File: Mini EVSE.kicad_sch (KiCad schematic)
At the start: 33 parts, among them IC1 G3MC-201PL DC5, IC2 IRM-03-5, IC3 ATtiny84-20P, IC4 TMR1-0522, IC5 SI8261BAC-C-IP, J1 RE OUT, J10 M, J2 AC IN, J4 ICP, J5 SWITCH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

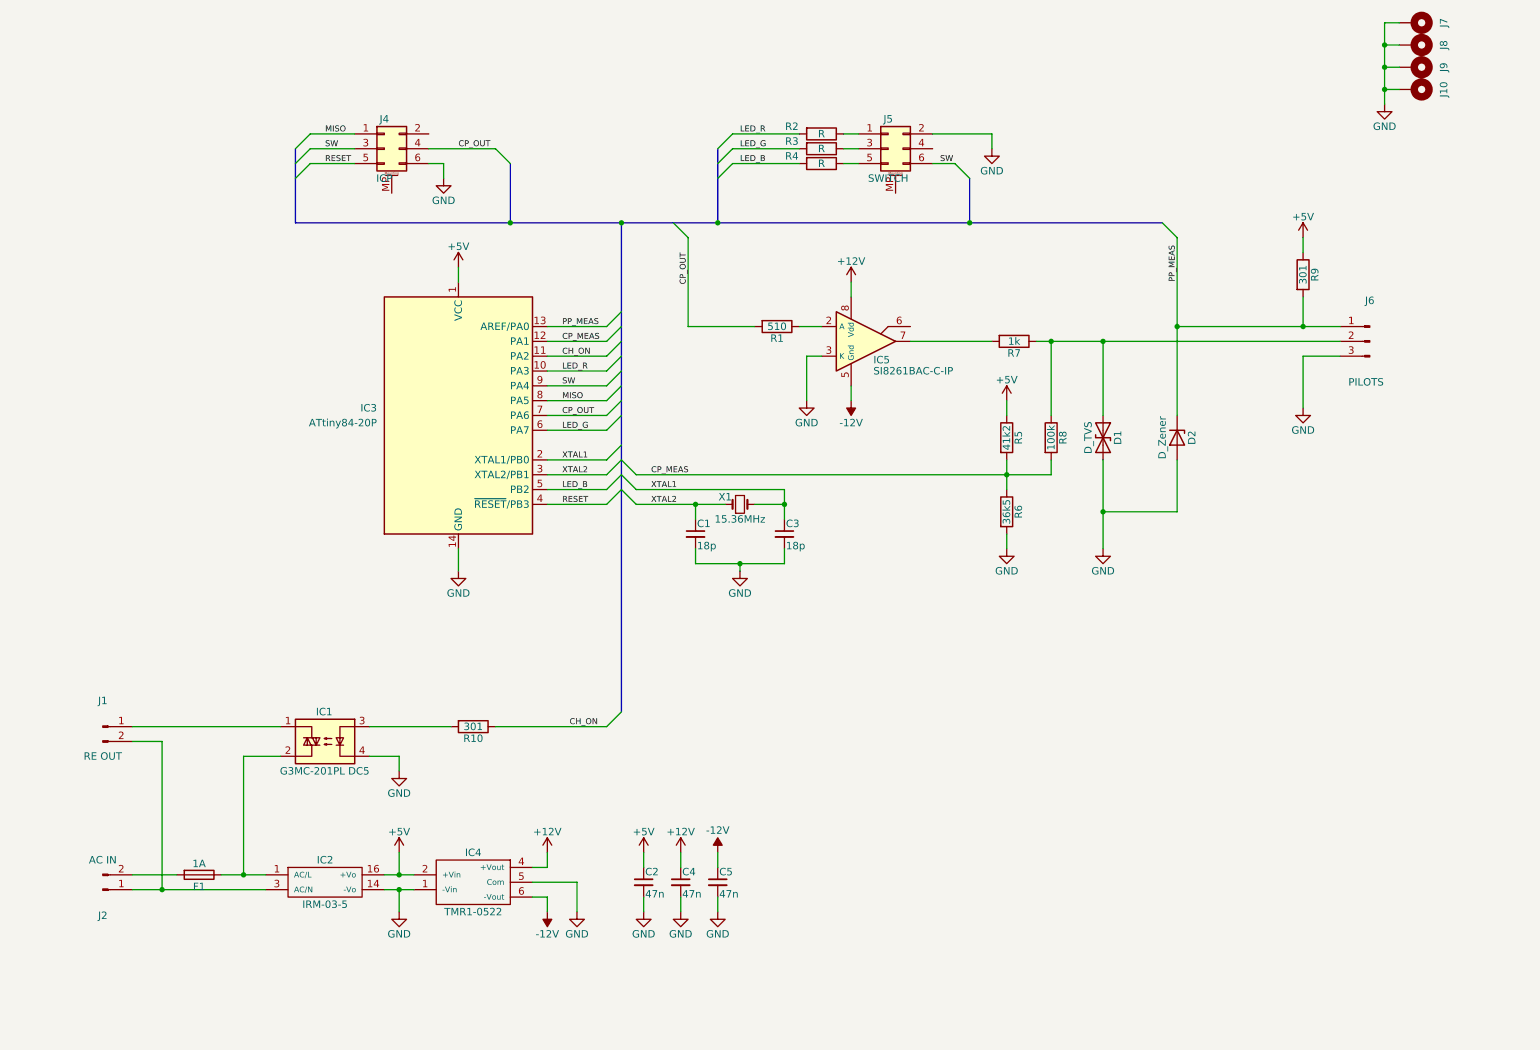
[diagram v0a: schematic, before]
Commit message: Changed supply to 24VDC with isolation
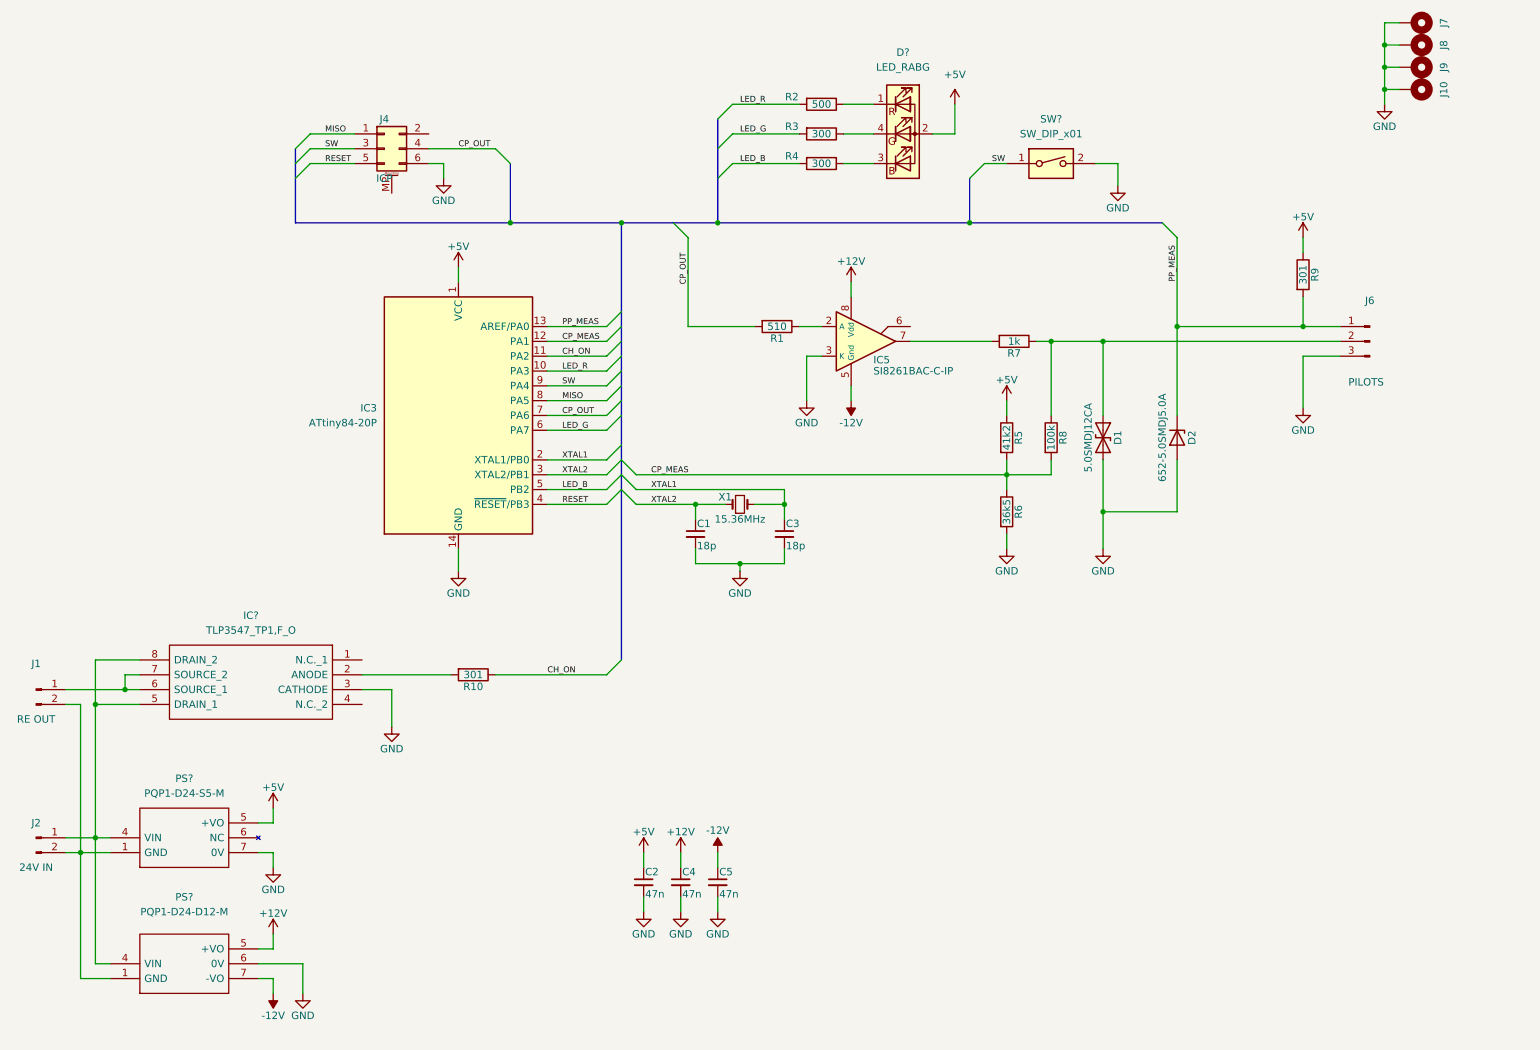
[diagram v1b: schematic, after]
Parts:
- removed F1: 1A, Fuse_Holders_and_Fuses:Fuseholder_Fuse_TR5_Littlefuse-No560_No460, symbol Device:Fuse
- removed IC1: G3MC-201PL DC5, Package_SIP:SIP4_Sharp-SSR_P7.62mm_Straight, symbol Relay_SolidState:S102S01
- removed IC2: IRM-03-5, Miscellaneous:MeanWell_IRM, symbol miscellaneous:IRM-03-5
- removed IC4: TMR1-0522, symbol miscellaneous:TMR1-0522
- removed J5: SWITCH, Pin_Headers:Pin_Header_Straight_2x03_Pitch2.54mm, symbol Connector_Generic_MountingPin:Conn_02x03_Odd_Even_MountingPin
- added D?: LED_RABG, symbol Device:LED_RABG
- added IC?: TLP3547_TP1,F_O, SOP254P1000X425-8N, symbol SamacSys_Parts:TLP3547_TP1,F_O
- added PS?: PQP1-D24-S5-M, PQP1D24S5M, symbol SamacSys_Parts:PQP1-D24-S5-M
- added PS?: PQP1-D24-D12-M, PQP1D24S5M, symbol SamacSys_Parts:PQP1-D24-S5-M
- added SW?: SW_DIP_x01, symbol Switch:SW_DIP_x01
- D1: value D_TVS -> 5.0SMDJ12CA
- D2: value D_Zener -> 652-5.0SMDJ5.0A
- J2: value AC IN -> 24V IN
- R2: value R -> 500
- R3, R4: value R -> 300
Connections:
- net +12V: now also PS?.5 (+VO)
- net +5V: now also D?.2 (A), PS?.5 (+VO)
- net -12V: now also PS?.7 (-VO)
- net GND: now also IC?.3 (CATHODE), PS?.6 (0V), PS?.7 (0V), SW?.2
- net SW: now also SW?.1
- net at J2.1 (Pin_1): now also IC?.5 (DRAIN_1), IC?.8 (DRAIN_2), PS?.4 (VIN), PS?.4 (VIN); no longer J1.2 (Pin_2)
- net at J2.2 (Pin_2): now also J1.2 (Pin_2), PS?.1 (GND), PS?.1 (GND)
- net at R2.1: now also D?.1 (RK)
- net at R3.1: now also D?.4 (GK)
- net at R4.1: now also D?.3 (BK)
- net at J1.1 (Pin_1): now also IC?.6 (SOURCE_1), IC?.7 (SOURCE_2)
- net at R10.2: now also IC?.2 (ANODE)
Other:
- moved on the sheet: J1, J2, R10, R2, R3

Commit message: Added PCB layout for DIN rail version
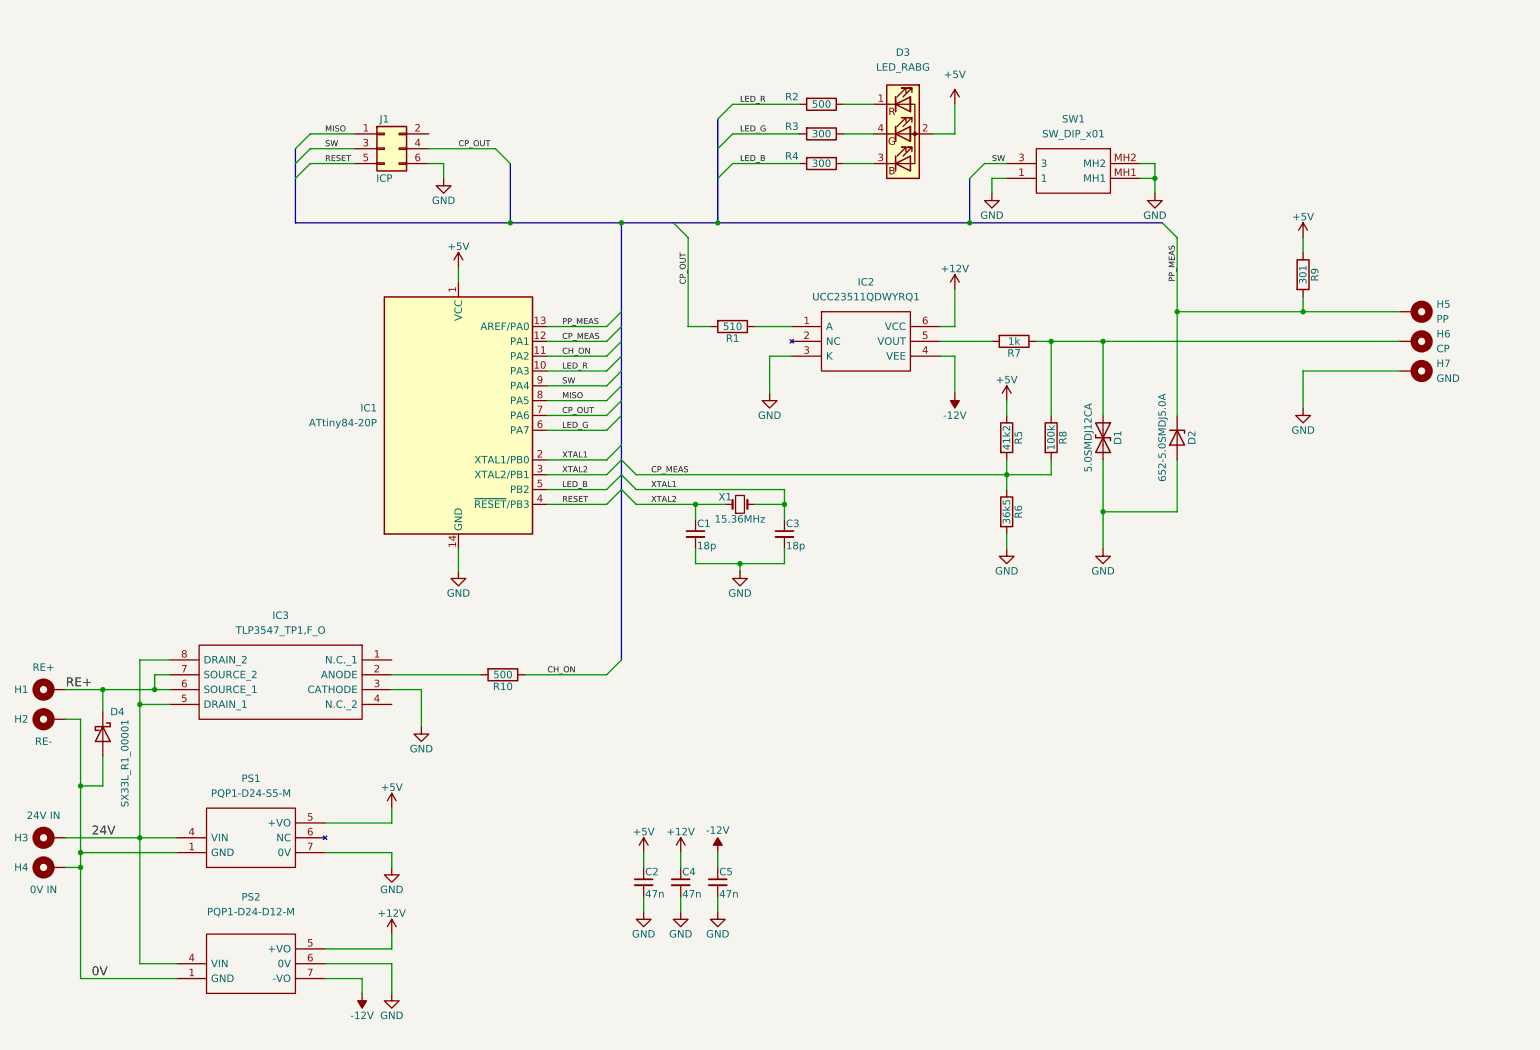
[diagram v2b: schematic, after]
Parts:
- removed IC5: SI8261BAC-C-IP, Housings_DIP:DIP-8_W7.62mm_LongPads, symbol miscellaneous:SI8261BAC-C-IP
- removed J1: RE OUT, Connectors_Terminal_Blocks:TerminalBlock_Pheonix_MKDS1.5-2pol, symbol Connector:Conn_01x02_Male
- removed J10, J7, J8, J9: M, Mounting_Holes:MountingHole_3.2mm_M3_ISO7380_Pad, symbol Mechanical:MountingHole_Pad
- removed J2: 24V IN, Connectors_Terminal_Blocks:TerminalBlock_Pheonix_MKDS1.5-2pol, symbol Connector:Conn_01x02_Male
- removed J6: PILOTS, Connectors_Terminal_Blocks:TerminalBlock_Pheonix_MKDS1.5-3pol, symbol Connector:Conn_01x03_Male
- added D4: SX33L_R1_00001, Diode_SMD:D_SMA_Handsoldering, symbol Device:D_Schottky
- added H1: RE+, TestPoint:TestPoint_Loop_D2.60mm_Drill1.4mm_Beaded, symbol Mechanical:MountingHole_Pad
- added H2: RE-, TestPoint:TestPoint_Loop_D2.60mm_Drill1.4mm_Beaded, symbol Mechanical:MountingHole_Pad
- added H3: 24V IN, TestPoint:TestPoint_Loop_D2.60mm_Drill1.4mm_Beaded, symbol Mechanical:MountingHole_Pad
- added H4: 0V IN, TestPoint:TestPoint_Loop_D2.60mm_Drill1.4mm_Beaded, symbol Mechanical:MountingHole_Pad
- added H5: PP, TestPoint:TestPoint_Loop_D2.60mm_Drill1.4mm_Beaded, symbol Mechanical:MountingHole_Pad
- added H6: CP, TestPoint:TestPoint_Loop_D2.60mm_Drill1.4mm_Beaded, symbol Mechanical:MountingHole_Pad
- added H7: GND, TestPoint:TestPoint_Loop_D2.60mm_Drill1.4mm_Beaded, symbol Mechanical:MountingHole_Pad
- added IC2: UCC23511QDWYRQ1, SamacSys_Parts:SOIC127P1150X355-6N, symbol SamacSys_Parts:UCC23511QDWYRQ1
- C1, C3: footprint Miscellaneous:C_Disc_D2.5mm_W3.2mm_P2.54mm -> Capacitor_SMD:C_1206_3216Metric_Pad1.33x1.80mm_HandSolder
- C2, C4, C5: footprint Miscellaneous:C_Disc_D5.1mm_W3.2mm_P5.08mm -> Capacitor_SMD:C_1206_3216Metric_Pad1.33x1.80mm_HandSolder
- D1, D2: footprint Diodes_THT:D_DO-201_P5.08mm_Vertical_KathodeUp -> Diode_SMD:D_SMC
- D3: renamed from D?; footprint (none) -> SamacSys_Parts:5504013F
- IC1: renamed from IC3; footprint Package_DIP:DIP-14_W7.62mm -> Package_SO:SOIC-14_3.9x8.7mm_P1.27mm
- IC3: renamed from IC?; footprint SOP254P1000X425-8N -> SamacSys_Parts:SOP254P1000X425-8N
- J1: renamed from J4; footprint Pin_Headers:Pin_Header_Straight_2x03_Pitch2.54mm -> Connector_PinHeader_2.54mm:PinHeader_2x03_P2.54mm_Vertical; symbol Connector_Generic_MountingPin:Conn_02x03_Odd_Even_MountingPin -> Connector_Generic:Conn_02x03_Odd_Even
- PS1, PS2: renamed from PS?; footprint PQP1D24S5M -> SamacSys_Parts:PQP1D24S5M
- R1, R2, R3, R4, R5, R6, R7, R8, R9: footprint Miscellaneous:R_Axial_DIN0207_L6.3mm_D2.5mm_P10.16mm_Horizontal -> Resistor_SMD:R_1210_3225Metric_Pad1.30x2.65mm_HandSolder
- R10: value 301 -> 500; footprint Miscellaneous:R_Axial_DIN0207_L6.3mm_D2.5mm_P10.16mm_Horizontal -> Resistor_SMD:R_1210_3225Metric_Pad1.30x2.65mm_HandSolder
- SW1: renamed from SW?; footprint (none) -> SamacSys_Parts:TPA11CGRA004; symbol Switch:SW_DIP_x01 -> SamacSys_Parts:TPA11CGRA004; Height (none) -> 5.994; Manufacturer_Name (none) -> TE Connectivity; Manufacturer_Part_Number (none) -> TPA11CGRA004; Mouser Part Number (none) -> 506-TPA11CGRA004; Mouser Price/Stock (none) -> https://www.mouser.co.uk/ProductDetail/TE-Connectivity-PB/T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
- X1: footprint Crystals:Crystal_HC49-U_Vertical -> Crystal:Crystal_HC49-U_Vertical
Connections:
- net +12V: now also IC2.6 (VCC)
- net -12V: now also IC2.4 (VEE)
- net GND: now also SW1.1, SW1.MH1, SW1.MH2, H7.1, IC2.3 (K); no longer SW1.2
- net PP_MEAS: now also H5.1
- net SW: now also SW1.3; no longer SW1.1
- net at R1.1: now also IC2.1 (A)
- net at R7.2: now also IC2.5 (VOUT)
- net at D1.1 (A1), R7.1, R8.1: now also H6.1
- net 24V: now reaches IC3.5 (DRAIN_1), IC3.8 (DRAIN_2), PS1.4 (VIN), PS2.4 (VIN)
- net 24V: now also H3.1
- net 0V: now reaches PS1.1 (GND), PS2.1 (GND)
- net 0V: now also D4.2 (A), H2.1, H4.1
- net RE+: now reaches IC3.6 (SOURCE_1), IC3.7 (SOURCE_2)
- net RE+: now also D4.1 (K), H1.1
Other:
- moved on the sheet: IC3, PS1, PS2, R1, R10

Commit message: Fixes to PCB layout - first prototype
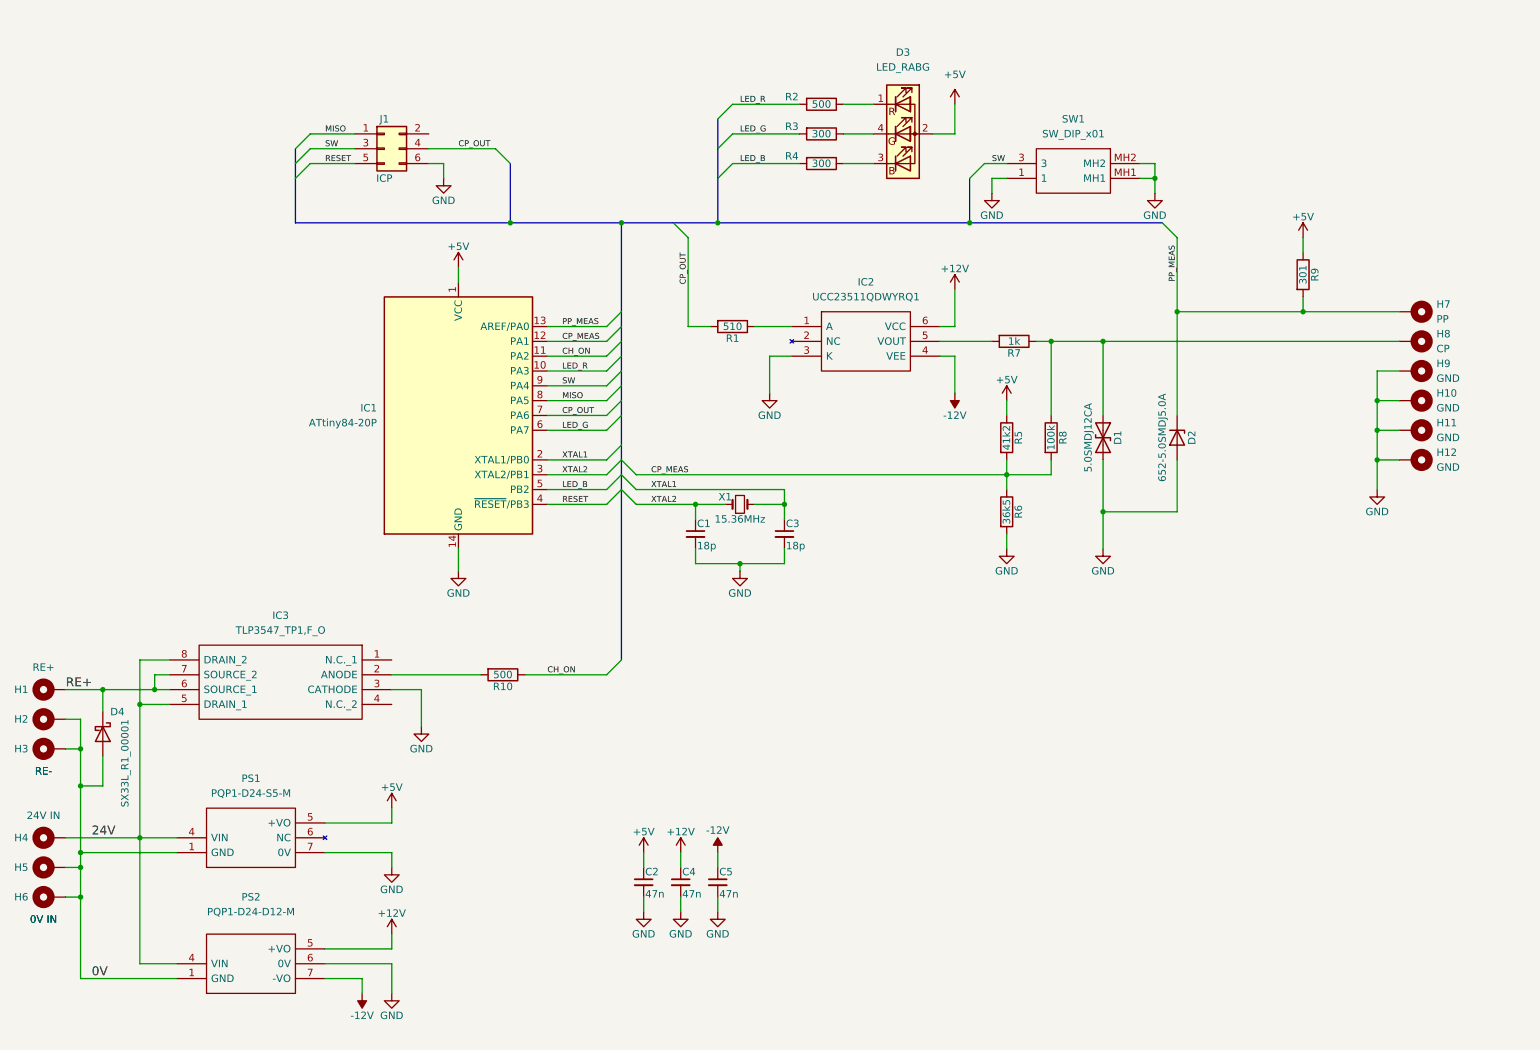
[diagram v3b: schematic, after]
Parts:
- added H10, H11, H12: GND, TestPoint:TestPoint_Loop_D2.60mm_Drill1.4mm_Beaded, symbol Mechanical:MountingHole_Pad
- added H3: RE-, TestPoint:TestPoint_Loop_D2.60mm_Drill1.4mm_Beaded, symbol Mechanical:MountingHole_Pad
- added H6: 0V IN, TestPoint:TestPoint_Loop_D2.60mm_Drill1.4mm_Beaded, symbol Mechanical:MountingHole_Pad
- renumbered H3 to H4, H4 to H5, H5 to H7, H6 to H8, H7 to H9
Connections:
- net 0V: now also H3.1, H6.1
- net GND: now also H10.1, H11.1, H12.1
